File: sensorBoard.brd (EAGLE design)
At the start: 20 x 50 mm, 25 parts, among them Q1 BSS84, U1 ADXL345, U2 L3G4200D, U3 MPL115A

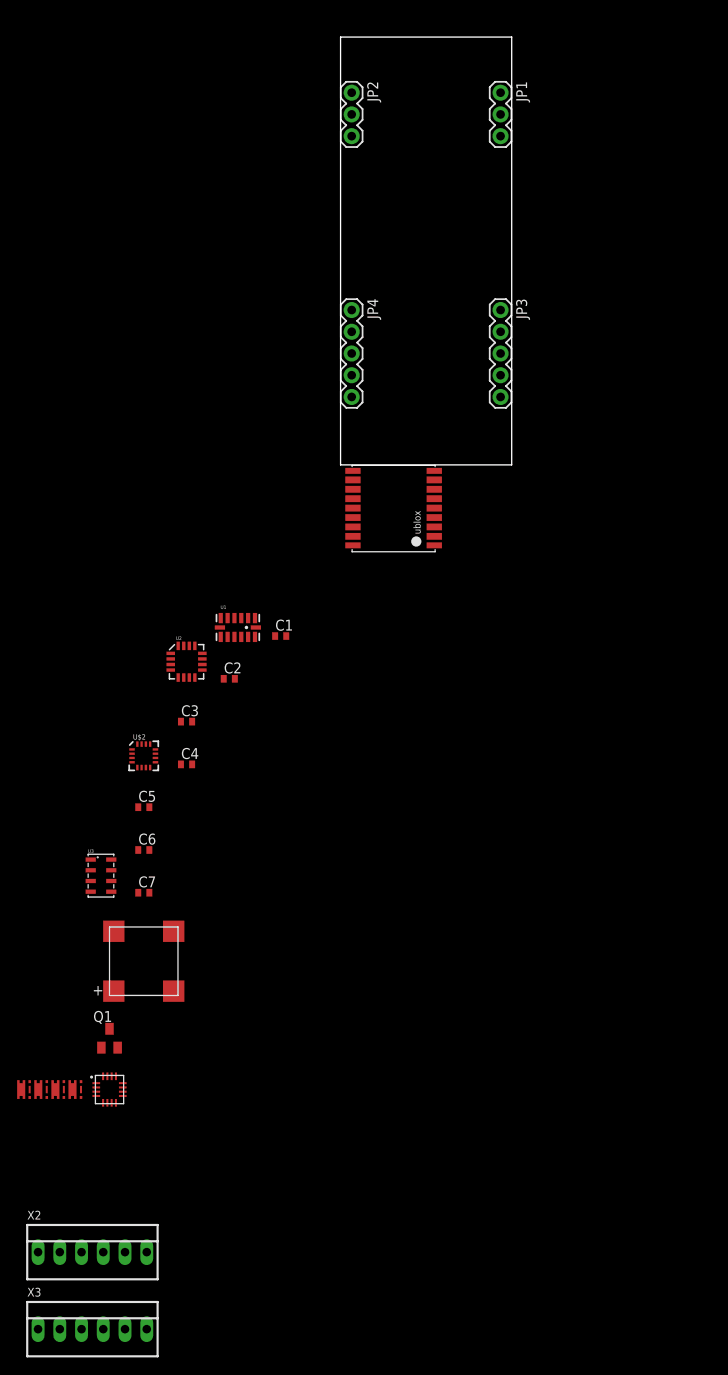
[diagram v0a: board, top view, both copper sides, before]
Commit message: Changed schematic, positioned components
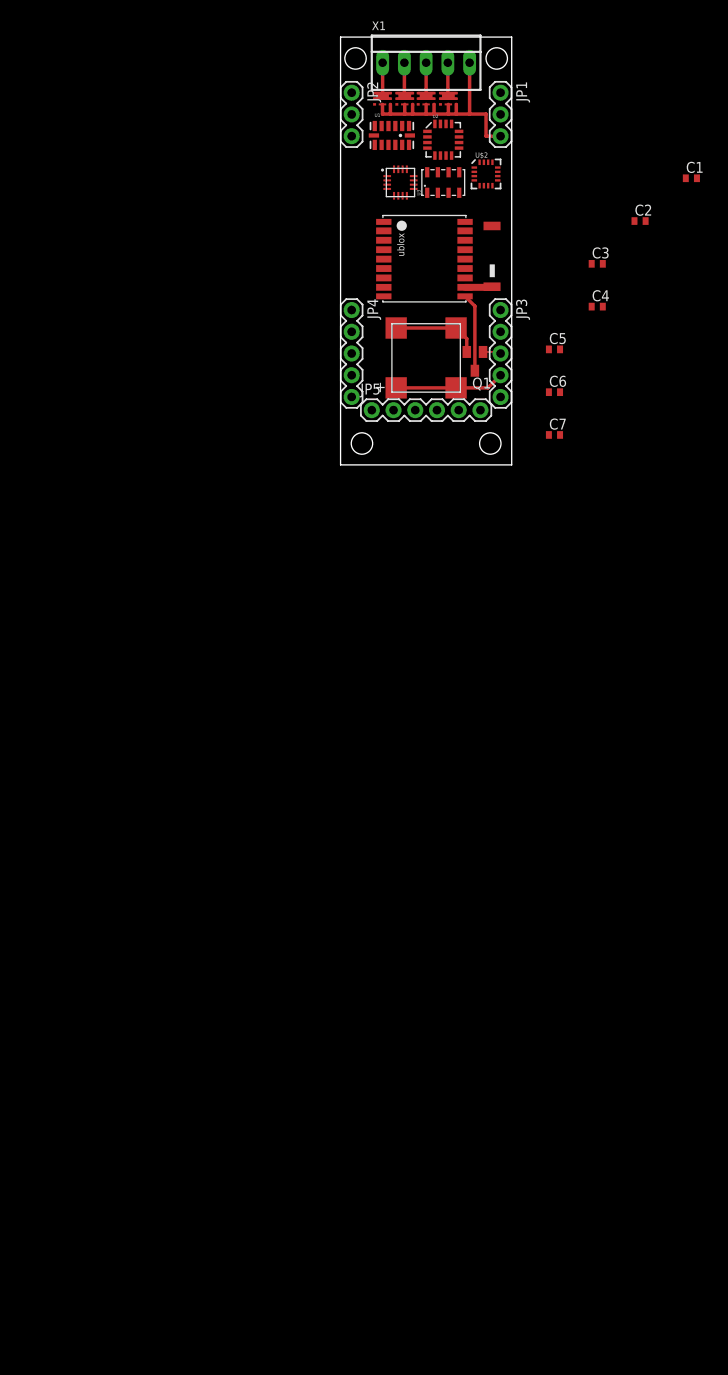
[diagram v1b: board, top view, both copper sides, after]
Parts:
- removed X2, X3: (no value), con-molex:22-23-2061
- added JP5: (no value), SparkFun:1X06
- added U$9: JTI_ANTENNA-1575AT43A40, Ava:JTI_ANTENNA-1575AT43A40
- added X1: 22-23-2051, con-molex:22-23-2051
- moved U$8 126.0 mm to (12.6, 42.8), turned to 270 degrees
- moved U$7 124.2 mm to (10.0, 42.8), turned to 270 degrees
- moved U$6 122.7 mm to (7.50, 42.8), turned to 270 degrees
- moved U$5 121.2 mm to (4.90, 42.8), turned to 270 degrees
- moved U$4 111.3 mm to (7.00, 33.0)
- moved U3 90.3 mm to (12.0, 33.0), turned to 90 degrees
- moved Q1 89.9 mm to (15.7, 12.1), turned to 180 degrees
- moved U$2 78.9 mm to (17.0, 34.0)
- moved U$3 77.8 mm to (10.0, 12.5)
- moved C1 71.9 mm to (41.0, 33.5)
- moved C2 71.9 mm to (35.0, 28.5)
- moved C3 71.9 mm to (30.0, 23.5)
- moved C4 71.9 mm to (30.0, 18.5)
- moved C5 71.9 mm to (25.0, 13.5)
- moved C6 71.9 mm to (25.0, 8.50)
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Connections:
- removed net V_BAT: X2.1, X3.1
- new net N$6: U$1.11_RF_IN, U$9.FEED
- net GND: now also X1.5; no longer X2.6, X3.6
- net GPIO1: now also JP5.5; no longer Q1.1
- net GPIO2: now also JP5.6
- net GPIO3: now also Q1.1
- net HP0: now also X1.1; no longer X2.2
- net HP1: now also X1.2; no longer X2.3
- net HP2: now also X1.3; no longer X2.4
- net HP3: now also X1.4; no longer X2.5
- net P4: now also JP5.1; no longer X3.2
- net P5: now also JP5.2; no longer X3.3
- net P6: now also JP5.3; no longer X3.4
- net P7: now also JP5.4; no longer X3.5
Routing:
- net GND: track 0.00 -> 40.6 mm
- net VBAT: track 0.00 -> 12.8 mm
- net N$5: track 0.00 -> 10.3 mm
- net HP3: track 0.00 -> 8.29 mm
- net HP1: track 0.00 -> 8.27 mm
- net HP0: track 0.00 -> 8.25 mm
- net HP2: track 0.00 -> 8.23 mm
- net N$6: track 0.00 -> 3.22 mm
- net GPIO3: track 0.00 -> 2.12 mm

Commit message: Board routing complete
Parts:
- added C8, C9: 100n, rcl:C0402
- moved C1 38.8 mm to (2.90, 26.2), turned to 90 degrees
- moved C2 31.4 mm to (5.80, 40.0)
- moved C7 30.3 mm to (18.9, 33.1), turned to 90 degrees
- moved C4 26.8 mm to (14.0, 40.0)
- moved C6 26.5 mm to (12.8, 32.0), turned to 270 degrees
- moved C3 25.4 mm to (10.7, 40.0), turned to 180 degrees
- moved C5 21.0 mm to (17.7, 33.1), turned to 90 degrees
- moved U$4 3.96 mm to (3.10, 32.3)
- moved U3 3.57 mm to (8.50, 32.3), turned to 180 degrees
- moved U$2 2.33 mm to (15.3, 32.4)
- moved U2 1.30 mm to (12.7, 36.9)
- moved U1 1.00 mm to (6.00, 37.5)
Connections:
- net GND: now also C8.2, C9.2
- net VCC: now also C8.1, C9.1
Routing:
- net VCC: track 0.00 -> 75.6 mm, vias 0 -> 7
- net GND: track 40.6 -> 111.7 mm, vias 0 -> 3
- net I2C_SCL: track 0.00 -> 34.1 mm, vias 0 -> 4
- net I2C_SDA: track 0.00 -> 29.7 mm, vias 0 -> 1
- net P7: track 0.00 -> 28.8 mm, vias 0 -> 1
- net GPS_TX: track 0.00 -> 28.2 mm, vias 0 -> 1
- net P6: track 0.00 -> 26.8 mm, vias 0 -> 1
- net P5: track 0.00 -> 25.3 mm, vias 0 -> 1
- net P4: track 0.00 -> 24.5 mm, vias 0 -> 1
- net P3: track 0.00 -> 18.6 mm, vias 0 -> 2
- net P2: track 0.00 -> 17.1 mm, vias 0 -> 2
- net GPIO1: track 0.00 -> 16.5 mm, vias 0 -> 1
- net P1: track 0.00 -> 16.4 mm, vias 0 -> 2
- net GPIO2: track 0.00 -> 15.2 mm, vias 0 -> 1
- net P0: track 0.00 -> 12.2 mm, vias 0 -> 2
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- added copper zone on layer 16, net GND
- added copper zone on layer 1, net N$7

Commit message: shuffled rf stuffs
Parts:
- added C10, C11: (no value), rcl:C0603
- moved U$9 23.9 mm to (9.90, 1.40), turned to 0 degrees
- moved JP5 21.1 mm to (3.65, 27.5)
- moved U$3 20.8 mm to (28.5, 21.9)
- moved Q1 10.7 mm to (14.7, 22.8), turned to 90 degrees
- moved U$1 9.30 mm to (10.0, 14.7), turned to 90 degrees
- moved C1 3.40 mm to (3.00, 22.9)
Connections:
- new net N$7: C10.2, C11.1, U$1.11_RF_IN
- net GND: now also C11.2
- net N$6: now also C10.1; no longer U$1.11_RF_IN
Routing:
- net VCC: track 75.6 -> 44.7 mm, vias 7 -> 5
- net P7: track 28.8 -> 0.00 mm, vias 1 -> 0
- net GPS_TX: track 28.2 -> 0.00 mm, vias 1 -> 0
- net P6: track 26.8 -> 0.00 mm, vias 1 -> 0
- net P5: track 25.3 -> 0.00 mm, vias 1 -> 0
- net P4: track 24.5 -> 0.00 mm, vias 1 -> 0
- net GPIO1: track 16.5 -> 0.00 mm, vias 1 -> 0
- net GPIO2: track 15.2 -> 0.00 mm, vias 1 -> 0
- net GPS_RX: track 11.3 -> 0.00 mm
- net GND: track 111.7 -> 102.4 mm, vias 3 -> 12
- net VBAT: track 12.8 -> 7.00 mm
- net N$5: track 10.3 -> 7.00 mm
- net N$7: track 0.00 -> 3.15 mm
- net GPIO3: track 2.12 -> 0.00 mm
- net N$6: track 3.22 -> 5.08 mm
- added copper zone on layer 1, net GND
- removed copper zone on layer 1, net N$7

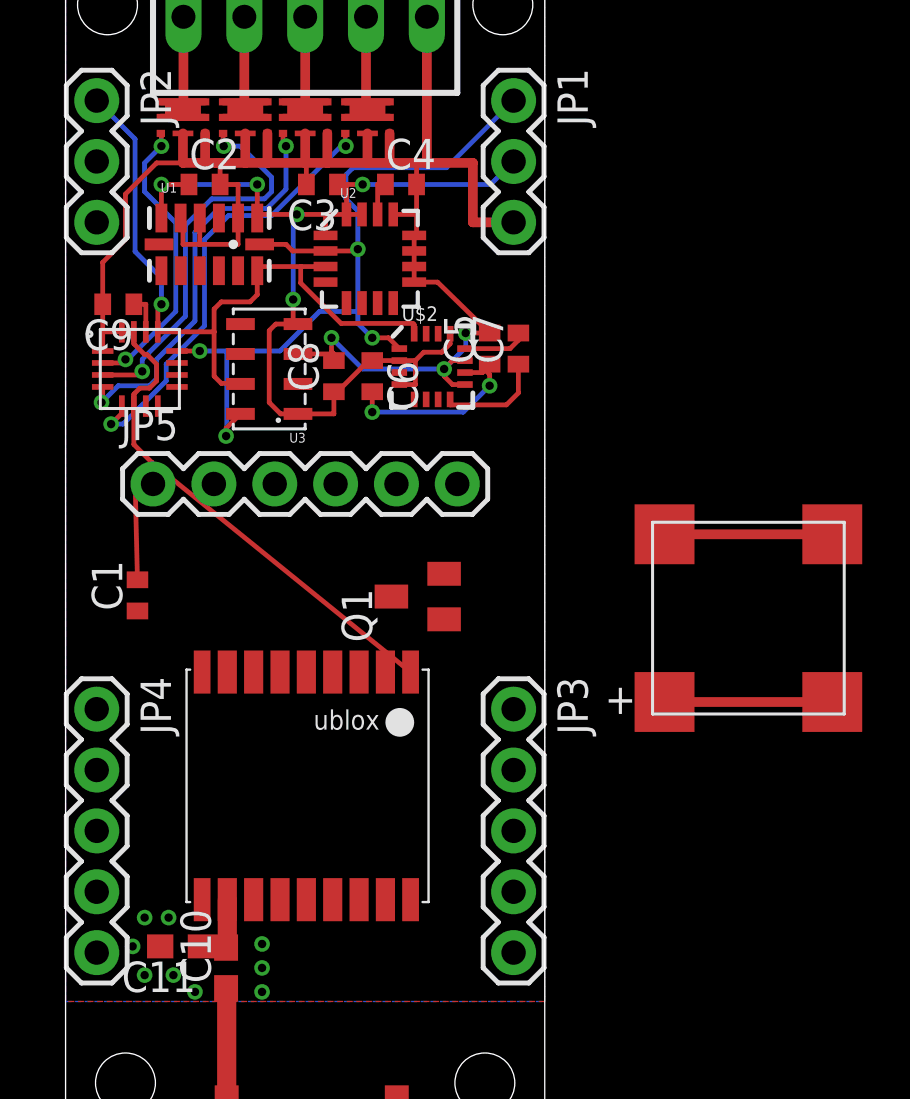
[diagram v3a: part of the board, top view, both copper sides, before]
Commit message: Changed buzzer routed lines
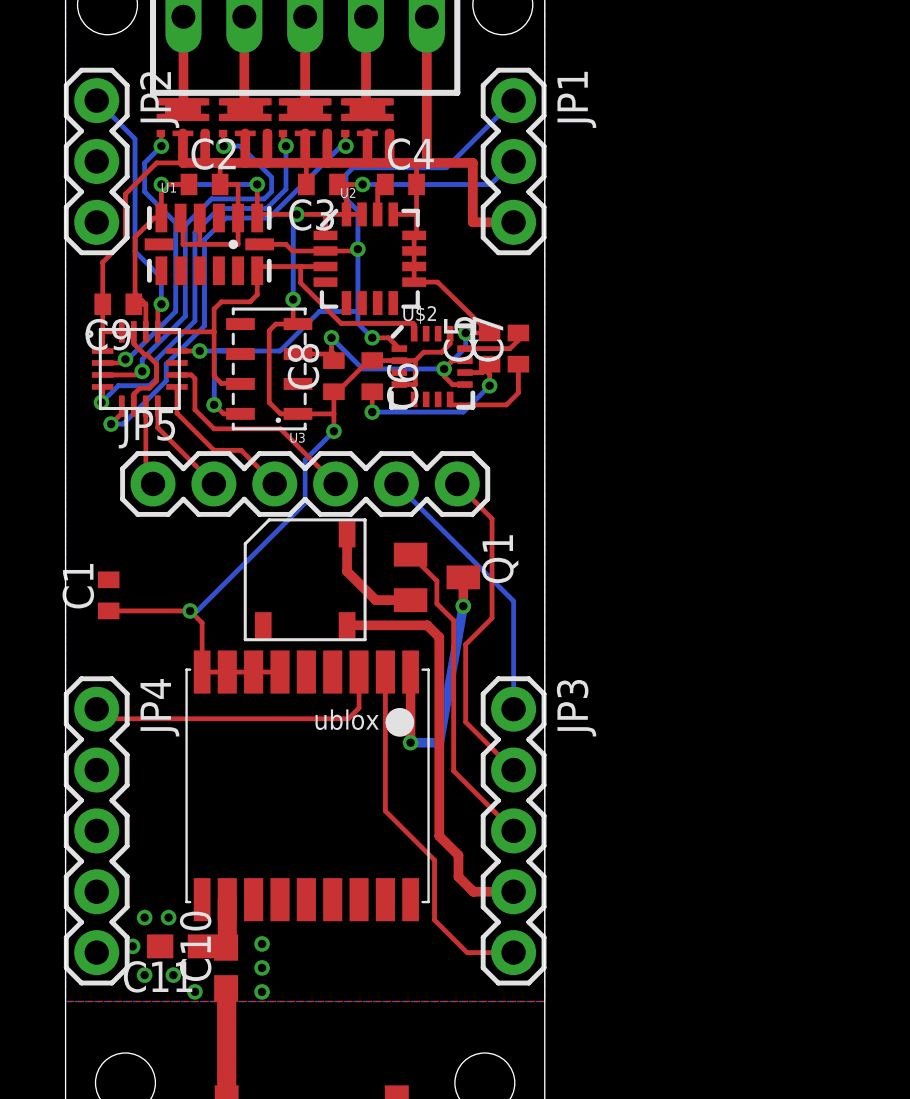
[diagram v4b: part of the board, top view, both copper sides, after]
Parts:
- U$3: value KSSG74B16 -> KSSG23J12; device mattsLib:KSSG74B16 -> mattsLib:KSSG23J12
- moved U$3 18.6 mm to (10.0, 23.5), turned to 90 degrees
- moved C1 1.20 mm to (1.80, 22.9)
- moved Q1 1.13 mm to (15.5, 23.6), turned to 270 degrees
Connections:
- net N$5: now also U$3.-; no longer U$3.P$2, U$3.P$3
- net VBAT: now also U$3.+; no longer U$3.P$1, U$3.P$4
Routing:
- net VCC: track 44.7 -> 69.4 mm, vias 5 -> 7
- net GPS_TX: track 0.00 -> 15.1 mm
- net GPIO2: track 0.00 -> 13.8 mm
- net GPIO3: track 0.00 -> 13.3 mm
- net GPS_RX: track 0.00 -> 12.8 mm
- net GPIO1: track 0.00 -> 11.4 mm
- net GND: track 102.4 -> 91.8 mm, vias 12 -> 14
- net VBAT: track 7.00 -> 16.9 mm
- net P7: track 0.00 -> 9.27 mm
- net P6: track 0.00 -> 6.40 mm
- net P5: track 0.00 -> 4.22 mm
- net P4: track 0.00 -> 3.37 mm
- net N$5: track 7.00 -> 4.70 mm
- net I2C_SCL: track 34.1 -> 33.4 mm

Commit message: Stuff checked, freeze design
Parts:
- added C12: 100n, rcl:C0402
- added C13: 470n, rcl:C0402
- added D1: BAT60J, diode:SOD323_ST
- added R1: 10k, rcl:R0402
- moved C8 0.70 mm to (11.9, 32.0)
- moved C6 0.20 mm to (13.0, 32.0)
- moved C5 0.10 mm to (17.8, 33.1)
- moved C7 0.10 mm to (19.0, 33.1)
- moved U$2 0.10 mm to (15.4, 32.4)
- moved U3 0.10 mm to (8.40, 32.3)
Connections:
- new net N$8: C12.1, U3.2
- new net N$9: C13.2, R1.2
- net GND: now also C12.2, R1.1, U1.12, U2.4, U2.8
- net N$1: now also C13.1
- net N$5: now also D1.A
- net VBAT: now also D1.C
- net VCC: now also U1.7, U2.5
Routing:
- net GND: track 91.8 -> 101.8 mm, vias 14 -> 15
- net VCC: track 69.4 -> 76.7 mm, vias 7 -> 8
- net VBAT: track 16.9 -> 23.2 mm
- net N$5: track 4.70 -> 10.00 mm
- net N$1: track 1.57 -> 5.65 mm
- net N$9: track 0.00 -> 1.80 mm
- net N$8: track 0.00 -> 1.46 mm
- net I2C_SDA: track 29.7 -> 30.8 mm

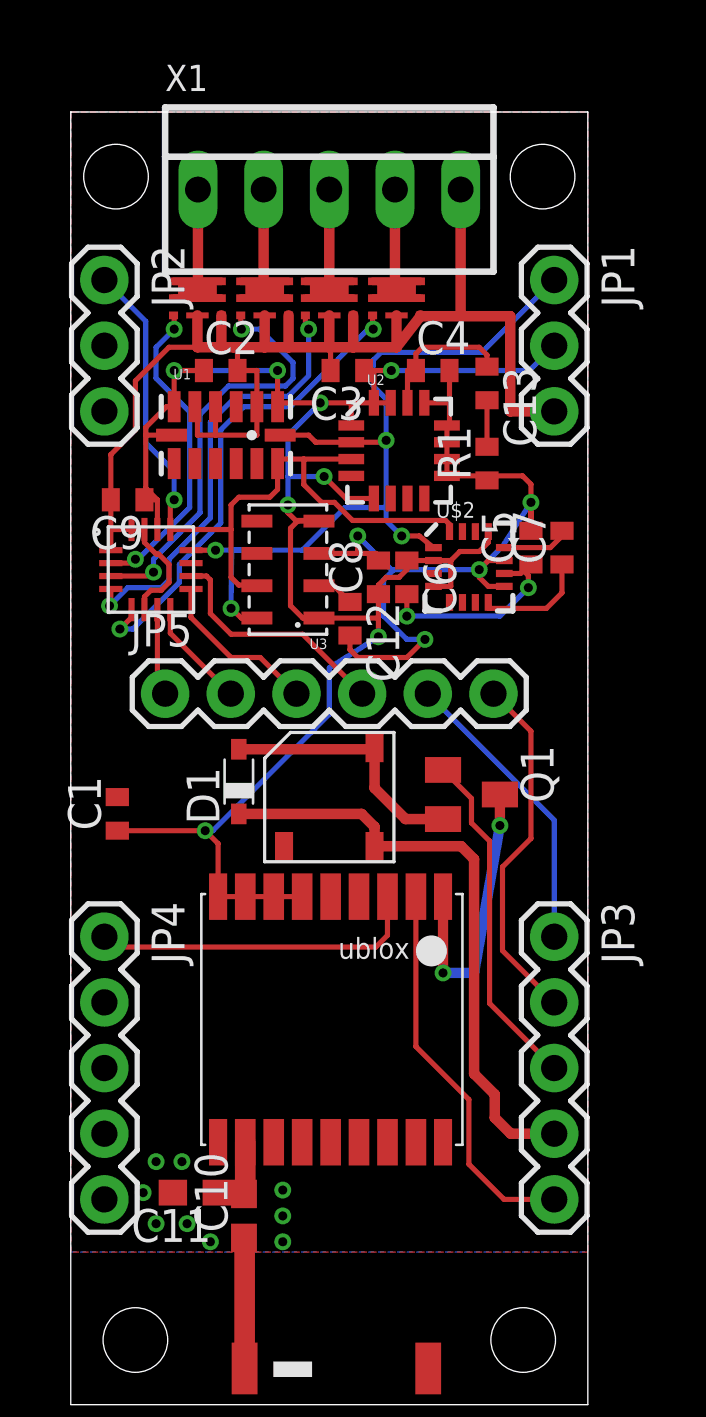
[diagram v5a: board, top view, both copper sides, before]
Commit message: Done silk for sensorboard.
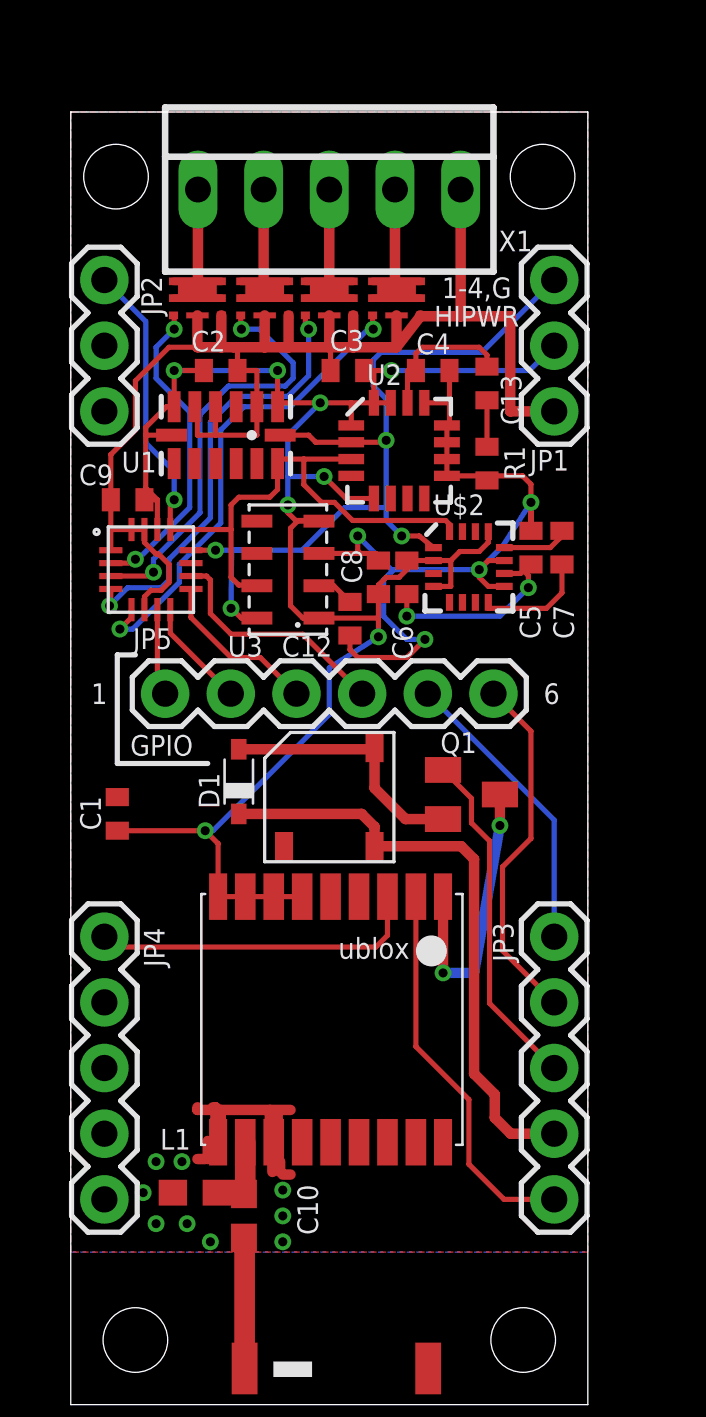
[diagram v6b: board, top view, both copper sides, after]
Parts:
- renumbered C11 to L1
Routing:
- net N$16: track 0.00 -> 3.70 mm
- net N$13: track 0.00 -> 1.20 mm
- net N$10: track 0.00 -> 1.00 mm
- net N$14: track 0.00 -> 0.70 mm
- net N$11: track 0.00 -> 0.60 mm
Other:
- board text added: "1"
- board text added: "1-4,G"
- board text added: "6"
- board text added: "GPIO"
- board text added: "HIPWR"
